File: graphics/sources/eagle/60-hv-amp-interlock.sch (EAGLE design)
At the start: 18 parts

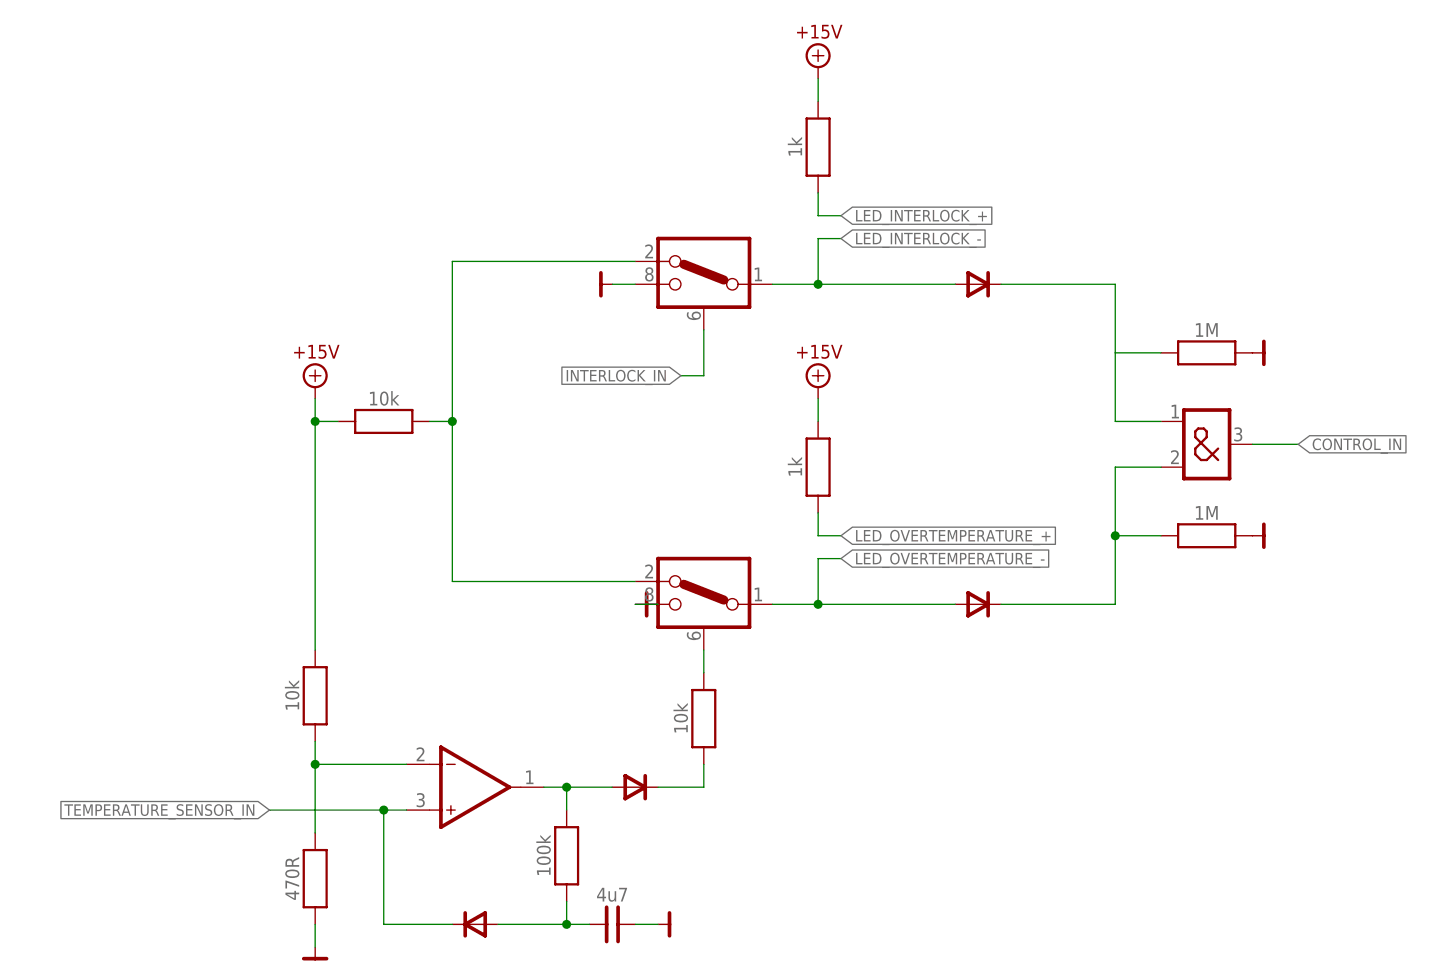
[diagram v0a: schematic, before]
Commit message: Added annotations to Eagle diagrams. Still needs textual updates.
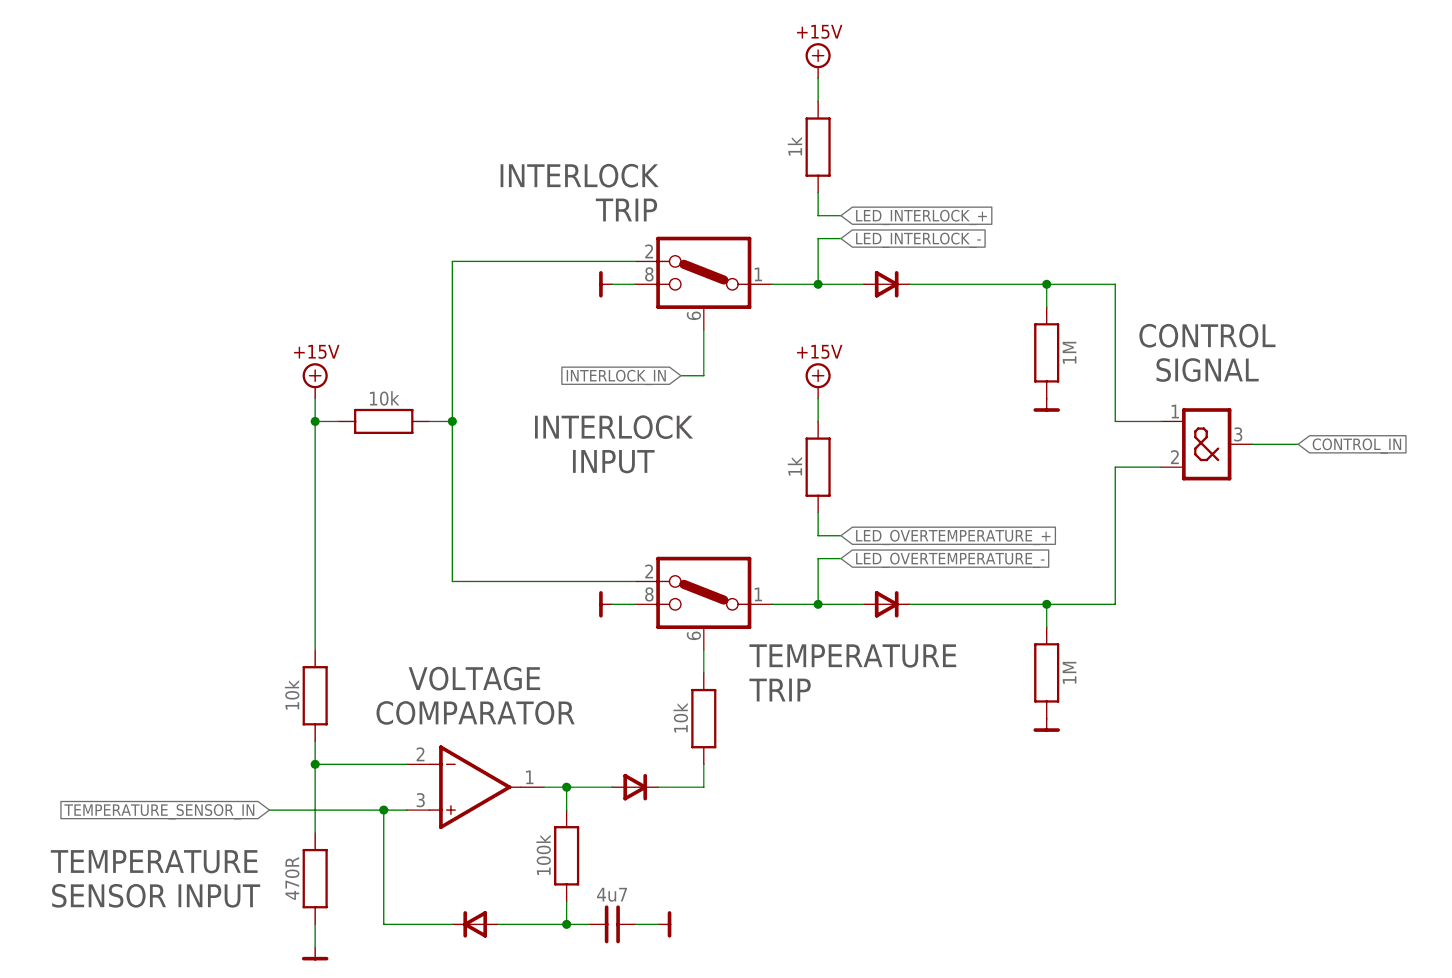
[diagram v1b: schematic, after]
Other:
- note added: "CONTROL SIGNAL"
- note added: "INTERLOCK INPUT"
- note added: "INTERLOCK TRIP"
- note added: "TEMPERATURE SENSOR INPUT"
- note added: "TEMPERATURE TRIP"
- note added: "VOLTAGE COMPARATOR"
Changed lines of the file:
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@@
 <setting verticaltext="up"/>
 </settings>
-<grid distance="0.1" unitdist="inch" unit="inch" style="lines" multiple="1" display="yes" altdistance="0.025" altunitdist="inch" altunit="inch"/>
+<grid distance="0.1" unitdist="inch" unit="inch" style="lines" multiple="1" display="no" altdistance="0.025" altunitdist="inch" altunit="inch"/>
 <layers>
 <layer number="91" name="Nets" color="34" fill="1" visible="yes" active="yes"/>
@@
 <sheet>
 <plain>
+<text x="147.32" y="180.34" size="2.54" layer="97" font="vector" align="center-left">TEMPERATURE
+TRIP</text>
+<text x="137.16" y="233.68" size="2.54" layer="97" font="vector" align="center-right">INTERLOCK
+TRIP</text>
+<text x="116.84" y="177.8" size="2.54" layer="97" font="vector" align="center">VOLTAGE
+COMPARATOR</text>
+<text x="198.12" y="215.9" size="2.54" layer="97" font="vector" align="center">CONTROL
+SIGNAL</text>
+<text x="81.28" y="157.48" size="2.54" layer="97" font="vector" align="center">TEMPERATURE
+SENSOR INPUT</text>
+<text x="132.08" y="205.74" size="2.54" layer="97" font="vector" align="center">INTERLOCK
+INPUT</text>
 </plain>
 <instances>
@@
 <instance part="$44" gate="A" x="132.08" y="223.52" rot="R270"/>
 <instance part="$46" gate="A" x="154.94" y="248.92"/>
-<instance part="$45" gate="A" x="137.16" y="187.96" rot="R270"/>
+<instance part="$45" gate="A" x="132.08" y="187.96" rot="R270"/>
 <instance part="N24" gate="A" x="198.12" y="205.74" smashed="yes"/>
 <instance part="$47" gate="A" x="154.94" y="213.36"/>
-<instance part="D25" gate="A" x="172.72" y="223.52" smashed="yes"/>
-<instance part="D26" gate="A" x="172.72" y="187.96" smashed="yes"/>
-<instance part="R150" gate="A" x="198.12" y="215.9" smashed="yes" rot="R180">
-<attribute name="VALUE" x="198.12" y="218.44" size="1.524" layer="96" font="vector" rot="R180" align="center"/>
-</instance>
-<instance part="R151" gate="A" x="198.12" y="195.58" smashed="yes" rot="R180">
-<attribute name="VALUE" x="198.12" y="198.12" size="1.524" layer="96" font="vector" rot="R180" align="center"/>
-</instance>
-<instance part="$210" gate="A" x="203.2" y="215.9" rot="R90"/>
-<instance part="$211" gate="A" x="203.2" y="195.58" rot="R90"/>
+<instance part="D25" gate="A" x="162.56" y="223.52" smashed="yes"/>
+<instance part="D26" gate="A" x="162.56" y="187.96" smashed="yes"/>
+<instance part="R150" gate="A" x="180.34" y="215.9" smashed="yes" rot="R90">
+<attribute name="VALUE" x="182.88" y="215.9" size="1.524" layer="96" font="vector" rot="R90" align="center"/>
+</instance>
+<instance part="R151" gate="A" x="180.34" y="180.34" smashed="yes" rot="R90">
+<attribute name="VALUE" x="182.88" y="180.34" size="1.524" layer="96" font="vector" rot="R90" align="center"/>
+</instance>
+<instance part="$210" gate="A" x="180.34" y="210.82"/>
+<instance part="$211" gate="A" x="180.34" y="175.26"/>
 </instances>
 <busses>
@@
 <pinref part="N23" gate="A" pin="S2B"/>
 <pinref part="$45" gate="A" pin="GND"/>
-<wire x1="134.62" y1="187.96" x2="137.16" y2="187.96" width="0.1524" layer="91"/>
+<wire x1="132.08" y1="187.96" x2="134.62" y2="187.96" width="0.1524" layer="91"/>
 </segment>
 <segment>
@@
 <wire x1="154.94" y1="223.52" x2="149.86" y2="223.52" width="0.1524" layer="91"/>
 <pinref part="D25" gate="A" pin="A"/>
-<wire x1="154.94" y1="223.52" x2="170.18" y2="223.52" width="0.1524" layer="91"/>
+<wire x1="154.94" y1="223.52" x2="160.02" y2="223.52" width="0.1524" layer="91"/>
 <junction x="154.94" y="223.52"/>
 </segment>
@@
 <wire x1="149.86" y1="187.96" x2="154.94" y2="187.96" width="0.1524" layer="91"/>
 <pinref part="D26" gate="A" pin="A"/>
-<wire x1="154.94" y1="187.96" x2="170.18" y2="187.96" width="0.1524" layer="91"/>
+<wire x1="154.94" y1="187.96" x2="160.02" y2="187.96" width="0.1524" layer="91"/>
 <junction x="154.94" y="187.96"/>
 </segment>
@@
 <pinref part="N24" gate="A" pin="I1"/>
 <wire x1="187.96" y1="208.28" x2="193.04" y2="208.28" width="0.1524" layer="91"/>
-<wire x1="187.96" y1="215.9" x2="187.96" y2="223.52" width="0.1524" layer="91"/>
-<wire x1="187.96" y1="215.9" x2="187.96" y2="208.28" width="0.1524" layer="91"/>
+<wire x1="187.96" y1="223.52" x2="187.96" y2="208.28" width="0.1524" layer="91"/>
+<pinref part="D25" gate="A" pin="C"/>
+<wire x1="187.96" y1="223.52" x2="180.34" y2="223.52" width="0.1524" layer="91"/>
 <pinref part="R150" gate="A" pin="2"/>
-<wire x1="193.04" y1="215.9" x2="187.96" y2="215.9" width="0.1524" layer="91"/>
-<pinref part="D25" gate="A" pin="C"/>
-<wire x1="187.96" y1="223.52" x2="175.26" y2="223.52" width="0.1524" layer="91"/>
+<wire x1="180.34" y1="223.52" x2="165.1" y2="223.52" width="0.1524" layer="91"/>
+<wire x1="180.34" y1="220.98" x2="180.34" y2="223.52" width="0.1524" layer="91"/>
+<junction x="180.34" y="223.52"/>
 </segment>
 </net>
@@
 <pinref part="D26" gate="A" pin="C"/>
 <wire x1="187.96" y1="203.2" x2="193.04" y2="203.2" width="0.1524" layer="91"/>
-<wire x1="175.26" y1="187.96" x2="187.96" y2="187.96" width="0.1524" layer="91"/>
-<wire x1="187.96" y1="187.96" x2="187.96" y2="195.58" width="0.1524" layer="91"/>
-<wire x1="187.96" y1="195.58" x2="187.96" y2="203.2" width="0.1524" layer="91"/>
+<wire x1="165.1" y1="187.96" x2="180.34" y2="187.96" width="0.1524" layer="91"/>
+<wire x1="180.34" y1="187.96" x2="187.96" y2="187.96" width="0.1524" layer="91"/>
+<wire x1="187.96" y1="187.96" x2="187.96" y2="203.2" width="0.1524" layer="91"/>
 <pinref part="R151" gate="A" pin="2"/>
-<wire x1="193.04" y1="195.58" x2="187.96" y2="195.58" width="0.1524" layer="91"/>
-<junction x="187.96" y="195.58"/>
+<wire x1="180.34" y1="185.42" x2="180.34" y2="187.96" width="0.1524" layer="91"/>
+<junction x="180.34" y="187.96"/>
 </segment>
 </net>
@@
 </schematic>
 </drawing>
+<compatibility>
+<note version="6.3" minversion="6.2.2" severity="warning">
+Since Version 6.2.2 text objects can contain more than one line,
+which will not be processed correctly with this version.
+</note>
+</compatibility>
 </eagle>

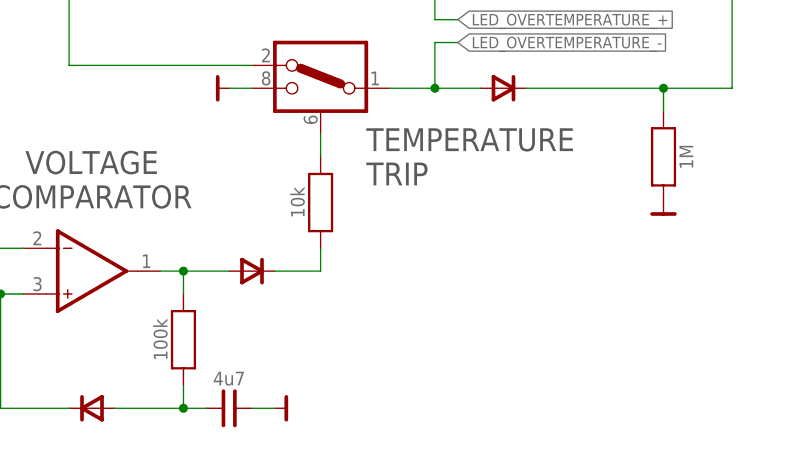
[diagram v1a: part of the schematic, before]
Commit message: Added ground reference to temperature interlock switch
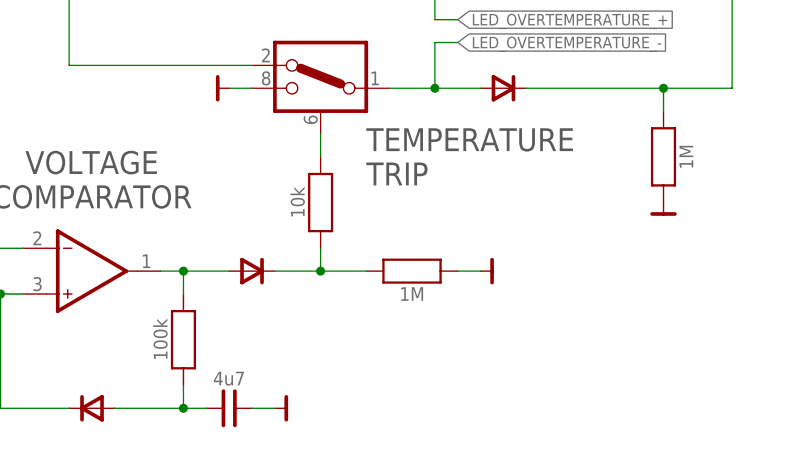
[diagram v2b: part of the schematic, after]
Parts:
- added R1: 1M, miscs:R04
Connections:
- net GND: now also R1.1
- net N$28: now also R1.2
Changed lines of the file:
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@@
 <part name="$210" library="signals" deviceset="VG" device=""/>
 <part name="$211" library="signals" deviceset="VG" device=""/>
+<part name="R1" library="miscs" deviceset="R" device="04" value="1M"/>
+<part name="$1" library="signals" deviceset="VG" device=""/>
 </parts>
 <sheets>
@@
 <instance part="$210" gate="A" x="180.34" y="210.82"/>
 <instance part="$211" gate="A" x="180.34" y="175.26"/>
+<instance part="R1" gate="A" x="152.4" y="167.64" smashed="yes" rot="R180">
+<attribute name="VALUE" x="152.4" y="165.1" size="1.524" layer="96" font="vector" rot="R180" align="center"/>
+</instance>
+<instance part="$1" gate="A" x="160.02" y="167.64" rot="R90"/>
 </instances>
 <busses>
@@
 <pinref part="R151" gate="A" pin="1"/>
 <pinref part="$211" gate="A" pin="GND"/>
+</segment>
+<segment>
+<pinref part="$1" gate="A" pin="GND"/>
+<pinref part="R1" gate="A" pin="1"/>
+<wire x1="160.02" y1="167.64" x2="157.48" y2="167.64" width="0.1524" layer="91"/>
 </segment>
 </net>
@@
 <wire x1="142.24" y1="167.64" x2="142.24" y2="170.18" width="0.1524" layer="91"/>
 <pinref part="R110" gate="A" pin="1"/>
-</segment>
-</net>
+<pinref part="R1" gate="A" pin="2"/>
+<wire x1="147.32" y1="167.64" x2="142.24" y2="167.64" width="0.1524" layer="91"/>
+<junction x="142.24" y="167.64"/>
+</segment>
+</net>
